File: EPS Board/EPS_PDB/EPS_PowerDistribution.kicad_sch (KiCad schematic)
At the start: 49 parts, among them U10 TPS259621DDAT, U11 LTC3624IDD-25PBF, U12 TPS259621DDAT, U13 TPS259621DDAT, U14 TPS259621DDAT, U15 TPS259621DDAT, U16 TPS259621DDAT, U17 LM5000-3MTCX, U18 AD7708BRUZ, U6 TPS259621DDAT, U7 TPS259621DDAT, U9 TPS259621DDAT

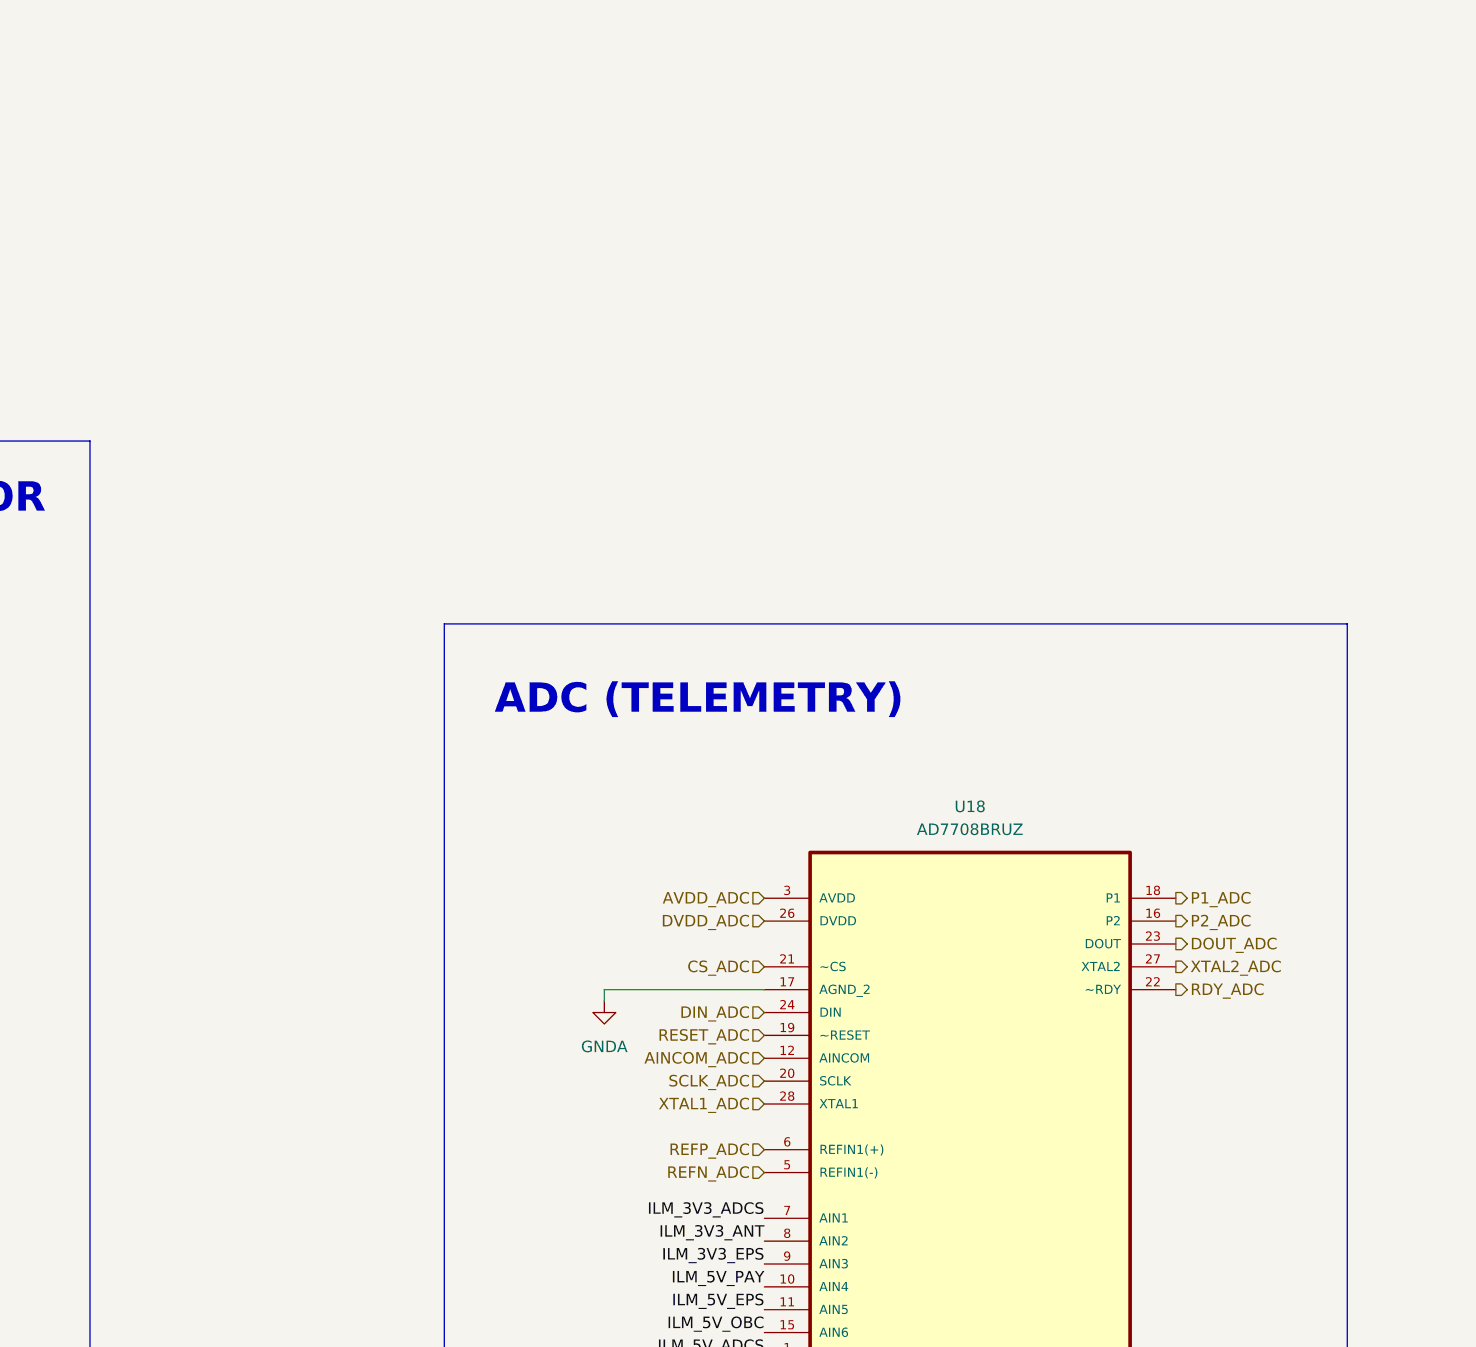
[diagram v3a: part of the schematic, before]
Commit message: Pin definitions of regulaton unit added to root and final changes commments added
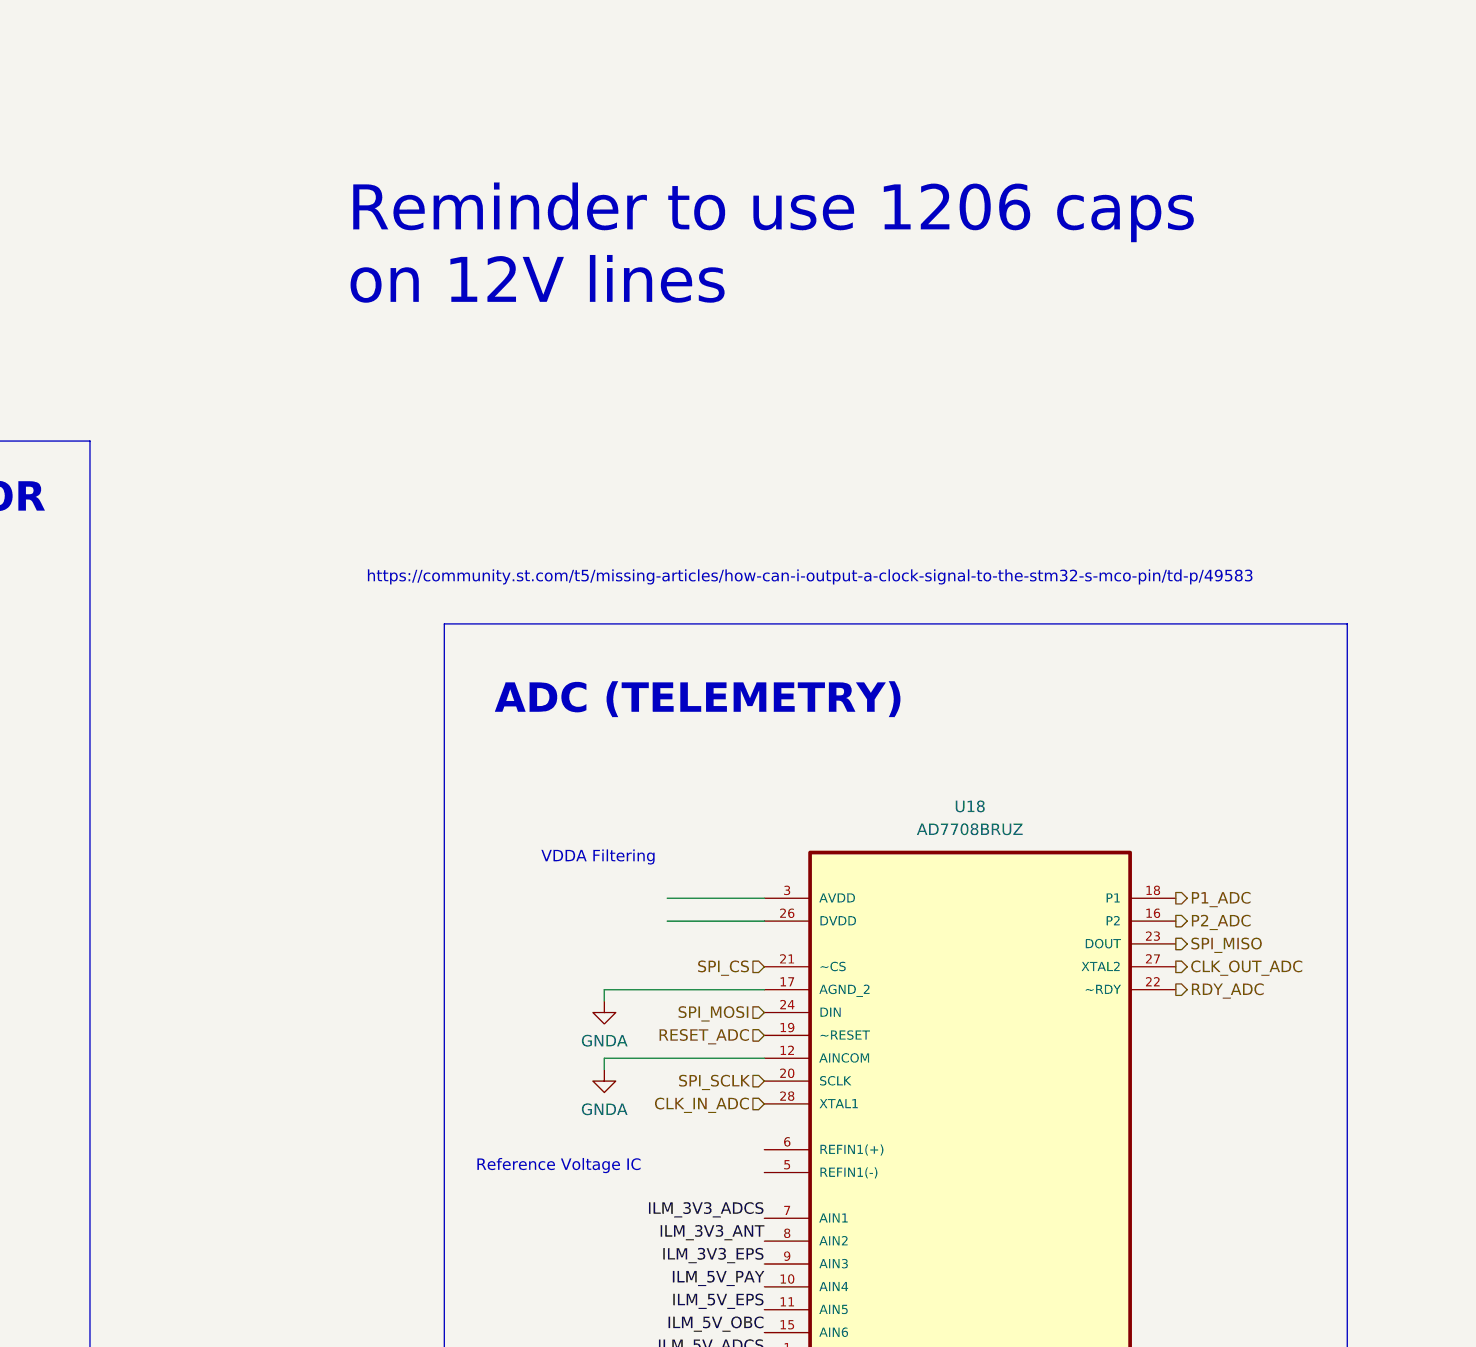
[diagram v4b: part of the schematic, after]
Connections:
- net AINCOM_ADC is gone; now on net GNDA: U18.12 (AINCOM)
- net AVDD_ADC: no longer names the net of U18.3 (AVDD)
- net CS_ADC renamed SPI_CS
- net DIN_ADC renamed SPI_MOSI
- net DOUT_ADC renamed SPI_MISO
- net DVDD_ADC: no longer names the net of U18.26 (DVDD)
- net REFN_ADC: no longer names the net of U18.5 (REFIN1(-))
- net REFP_ADC: no longer names the net of U18.6 (REFIN1(+))
- net SCLK_ADC renamed SPI_SCLK
- net XTAL1_ADC renamed CLK_IN_ADC
- net XTAL2_ADC renamed CLK_OUT_ADC
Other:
- note added: "Reference Voltage IC"
- note added: "Reminder to use 1206 caps on 12V lines"
- note added: "VDDA Filtering"
- note added: "https://community.st.com/t5/missing-articles/how-can-i-output-a-clock-signal-to-the-stm32-s-mco-pin/td-p/49583"
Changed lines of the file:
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@@
 	(wire
 		(pts
+			(xy 338.455 138.43) (xy 349.25 138.43)
+		)
+		(stroke
+			(width 0)
+			(type default)
+		)
+	)
+	(wire
+		(pts
 			(xy 148.59 73.66) (xy 148.59 72.39)
 		)
@@
 	(wire
 		(pts
+			(xy 338.455 140.97) (xy 349.25 140.97)
+		)
+		(stroke
+			(width 0)
+			(type default)
+		)
+	)
+	(wire
+		(pts
 			(xy 210.82 142.24) (xy 224.79 142.24)
 		)
@@
 	(wire
 		(pts
+			(xy 331.47 156.21) (xy 331.47 157.48)
+		)
+		(stroke
+			(width 0)
+			(type default)
+		)
+	)
+	(wire
+		(pts
 			(xy 200.66 237.49) (xy 204.47 237.49)
 		)
@@
 	(wire
 		(pts
+			(xy 349.25 156.21) (xy 331.47 156.21)
+		)
+		(stroke
+			(width 0)
+			(type default)
+		)
+	)
+	(wire
+		(pts
 			(xy 80.01 115.57) (xy 80.01 114.3)
 		)
@@
 		)
 	)
+	(text "Reference Voltage IC"
+		(exclude_from_sim no)
+		(at 326.39 168.275 0)
+		(effects
+			(font
+				(size 1.27 1.27)
+			)
+		)
+	)
 	(text "VOLTAGE CONVERTER/REGULATOR"
 		(exclude_from_sim no)
@@
 		)
 	)
+	(text "Reminder to use 1206 caps\non 12V lines"
+		(exclude_from_sim no)
+		(at 302.895 73.025 0)
+		(effects
+			(font
+				(size 5 5)
+			)
+			(justify left bottom)
+		)
+	)
 	(text "EPS DISTRIBUTION & REGULATION UNIT"
 		(exclude_from_sim no)
@@
 		)
 	)
+	(text "VDDA Filtering"
+		(exclude_from_sim no)
+		(at 330.835 133.985 0)
+		(effects
+			(font
+				(size 1.27 1.27)
+			)
+		)
+	)
+	(text "https://community.st.com/t5/missing-articles/how-can-i-output-a-clock-signal-to-the-stm32-s-mco-pin/td-p/49583"
+		(exclude_from_sim no)
+		(at 354.33 102.87 0)
+		(effects
+			(font
+				(size 1.27 1.27)
+			)
+		)
+	)
 	(text "CURRENT LIMITER"
 		(exclude_from_sim no)
@@
 		)
 	)
-	(hierarchical_label "XTAL1_ADC"
+	(hierarchical_label "CLK_IN_ADC"
 		(shape input)
 		(at 349.25 161.29 180)
@@
 		)
 	)
-	(hierarchical_label "XTAL2_ADC"
+	(hierarchical_label "CLK_OUT_ADC"
 		(shape output)
 		(at 394.97 146.05 0)
@@
 		)
 	)
-	(hierarchical_label "CS_ADC"
+	(hierarchical_label "SPI_CS"
 		(shape input)
 		(at 349.25 146.05 180)
@@
 		)
 	)
-	(hierarchical_label "AVDD_ADC"
-		(shape input)
-		(at 349.25 138.43 180)
-		(fields_autoplaced yes)
-		(effects
-			(font
-				(size 1.27 1.27)
-			)
-			(justify right)
-		)
-	)
 	(hierarchical_label "5V_OBC"
 		(shape output)
@@
 		)
 	)
-	(hierarchical_label "REFN_ADC"
-		(shape input)
-		(at 349.25 168.91 180)
-		(fields_autoplaced yes)
-		(effects
-			(font
-				(size 1.27 1.27)
-			)
-			(justify right)
-		)
-	)
-	(hierarchical_label "DIN_ADC"
+	(hierarchical_label "SPI_MOSI"
 		(shape input)
 		(at 349.25 151.13 180)
@@
 		)
 	)
-	(hierarchical_label "AINCOM_ADC"
-		(shape input)
-		(at 349.25 156.21 180)
-		(fields_autoplaced yes)
-		(effects
-			(font
-				(size 1.27 1.27)
-			)
-			(justify right)
-		)
-	)
 	(hierarchical_label "EN_3V3_ADCS"
 		(shape input)
@@
 		)
 	)
-	(hierarchical_label "DVDD_ADC"
-		(shape input)
-		(at 349.25 140.97 180)
-		(fields_autoplaced yes)
-		(effects
-			(font
-				(size 1.27 1.27)
-			)
-			(justify right)
-		)
-	)
 	(hierarchical_label "RESET_ADC"
 		(shape input)
@@
 		)
 	)
-	(hierarchical_label "SCLK_ADC"
+	(hierarchical_label "SPI_SCLK"
 		(shape input)
 		(at 349.25 158.75 180)
@@
 		)
 	)
-	(hierarchical_label "DOUT_ADC"
+	(hierarchical_label "SPI_MISO"
 		(shape output)
 		(at 394.97 143.51 0)
@@
 		)
 	)
-	(hierarchical_label "REFP_ADC"
-		(shape input)
-		(at 349.25 166.37 180)
-		(fields_autoplaced yes)
-		(effects
-			(font
-				(size 1.27 1.27)
-			)
-			(justify right)
-		)
-	)
 	(symbol
 		(lib_id "EPS_Schematic_v2-eagle-import:GND-EARTH")
@@
 		(on_board yes)
 		(dnp no)
-		(fields_autoplaced yes)
 		(property "Reference" "#PWR038"
 			(at 331.47 156.21 0)
@@
 		)
 		(property "Value" "GNDA"
-			(at 331.47 154.94 0)
+			(at 331.47 154.305 0)
 			(effects
 				(font
@@
 					(unit 1)
 				)
+			)
+		)
+	)
+	(symbol
+		(lib_id "power:GNDA")
+		(at 331.47 157.48 0)
+		(unit 1)
+		(exclude_from_sim no)
+		(in_bom yes)
+		(on_board yes)
+		(dnp no)
+		(property "Reference" "#PWR040"
+			(at 331.47 163.83 0)
+			(effects
+				(font
+					(size 1.27 1.27)
+				)
+				(hide yes)
+			)
+		)
+		(property "Value" "GNDA"
+			(at 331.47 161.925 0)
+			(effects
+				(font
+					(size 1.27 1.27)
+				)
+			)
+		)
+		(property "Footprint" ""
+			(at 331.47 157.48 0)
+			(effects
+				(font
+					(size 1.27 1.27)
+				)
+				(hide yes)
+			)
+		)
+		(property "Datasheet" ""
+			(at 331.47 157.48 0)
+			(effects
+				(font
+					(size 1.27 1.27)
+				)
+				(hide yes)
+			)
+		)
+		(property "Description" "Power symbol creates a global label with name \"GNDA\" , analog ground"
+			(at 331.47 157.48 0)
+			(effects
+				(font
+					(size 1.27 1.27)
+				)
+				(hide yes)
+			)
+		)
+		(pin "1"
+		)
+		(instances
+			(project "EPS_PDB"
+				(path "/b6081578-ab04-44e2-a71a-4911a5b750e4/2d9f4680-6d7b-4671-a50c-25972cd78742"
+					(reference "#PWR040")
+					(unit 1)
+				)

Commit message: Interfaced Control and PD&R unit
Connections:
- net GND: no longer R15.2
- net 12V_SHDN renamed SHDN_12V
- net 3V3_STATUS renamed STATUS_3V3
- net 5V_STATUS renamed STATUS_5V
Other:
- note added: "ADD CLOCK"
- note removed: "https://community.st.com/t5/missing-articles/how-can-i-output-a-clock-signal-to-the-stm32-s-mco-pin/td-p/49583"

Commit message: Reference voltage ic, clock, ADC schematic done
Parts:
- added 120R3: FerriteBead, symbol Device:FerriteBead
- added C29, C30: 10pF, symbol Device:C
- added C31, C34: C, symbol Device:C
- added C32, C33: 10uF, symbol Device:C
- added C35: 10nF, symbol Device:C
- added C36, C37: 1uF, symbol Device:C
- added JP5: Jumper_3_Bridged12, symbol Jumper:Jumper_3_Bridged12
- added R23: 130k, symbol Device:R
- added U2: TS4061BICT-1.25, SOT323-3L_1P35X2P2X0P65_STM, symbol TS4061BICT:TS4061BICT-1.25
- added Y4: 32.768kHz, symbol Device:Crystal
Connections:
- net 3V3_EPS is gone; now on net +3.3V: U13.5 (OUT)
- net GNDD is gone; now on net GND: U18.25 (DGND)
- net CLK_IN_ADC: now also C29.1, Y4.1
- net CLK_OUT_ADC: now also C30.1, Y4.2
- net GND: now also U18.5 (REFIN1(-)), C29.2, C30.2, C31.2, C32.2, C33.2, C34.2, C35.2, C36.2, C37.2, U2.2 (ANODE)
- net RESET_ADC: now also JP5.1 (A), JP5.3 (B)
- net +3.3V: now reaches U18.26 (DVDD)
- net +3.3V: now also 120R3.2, C33.1, C34.1, C37.1, JP5.2 (C), R23.1
- net +3.3VA: now reaches U18.3 (AVDD)
- net +3.3VA: now also 120R3.1, C35.1, C36.1
- net 1.25VREF: now reaches U18.6 (REFIN1(+))
- net 1.25VREF: now also C31.1, C32.1, R23.2, U2.1 (CATHODE)
- net P1_ADC: no longer names the net of U18.18 (P1)
- net P2_ADC: no longer names the net of U18.16 (P2)
- no-connect marks 12 -> 15
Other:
- note added: "15mA > (3.3-1.25)/R > 10uA (min input current) 136.67 Ohm < R < 205 kOhm"
- note added: "32.768 kHz CLK"
- note added: "Digital input used to reset the ADC to its power-on-reset status. This pin has a weak pull-up internally to DVDD"
- note added: "Load Capacitance = (12.5-5)*2 = 15pF [12.5pF (Datasheet) - Stray Capacitance (approx 5pF)]*2"
- note added: "REF pin consumes 0.5uA current"
- note added: "REFERENCE VOLTAGE"
- note added: "Try to use pads to solder connections instead of jumpers"
- note removed: "ADD CLOCK"
- note removed: "Reference Voltage IC"
- moved on the sheet: C17, C18, C19, C20, C21, C22, C23, C24, C25, C26, C27, C28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

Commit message: Added pull up resistors for current limiter
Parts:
- added D4: D_Schottky, symbol Device:D_Schottky
- added R24, R25, R26, R27, R28, R37, R38, R39, R40: 10k, Resistor_SMD:R_0603_1608Metric_Pad0.98x0.95mm_HandSolder, symbol EPS_Schematic_v2-eagle-import:R-USCHIP-0805(2012-METRIC)
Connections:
- net 3.3V_BUS: now also R24.2, R25.2, R26.2, R27.2, R28.2, R37.2, R38.2, R39.2, R40.2
- net 5V_ADCS: now also D4.1 (K)
- net FLT_12V_ADCS: now also R40.1
- net FLT_3V3_ADCS: now also R24.1
- net FLT_3V3_ANT: now also R25.1
- net FLT_3V3_EPS: now also R26.1
- net FLT_5V_ADCS: now also R38.1
- net FLT_5V_COMM: now also R39.1
- net FLT_5V_EPS: now also R28.1
- net FLT_5V_OBC: now also R37.1
- net FLT_5V_PAY: now also R27.1
- net GND: now also D4.2 (A)
- net at C22.2, JP2.3 (B), U11.6 (INTVCC): no longer JP2.2 (C), U11.7 (MODE/SYNC)
- net at C17.2, JP3.3 (B), U8.9 (INTVCC): no longer JP3.2 (C), U8.10 (MODE/SYNC)
- new net: JP2.2 (C), U11.7 (MODE/SYNC)
- new net: JP3.2 (C), U8.10 (MODE/SYNC)
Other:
- note added: "CLOCK"
- note added: "CURRENT LIMITER EXTRA CONNECTIONS"
- note added: "Need to connect 3.3V or 3.3VA to the 3.3V bus??"
- moved on the sheet: C29, C30, R14, R18, R21, R22, Y4
